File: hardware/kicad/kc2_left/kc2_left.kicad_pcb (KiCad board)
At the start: 2 copper layers, 145.7 x 132.2 mm, 76 parts, among them SW1 KEY_01, SW10 KEY_10, SW11 KEY_11, SW12 KEY_12, SW13 KEY_13, SW14 KEY_14, SW15 KEY_15, SW16 KEY_16, SW17 KEY_17, SW18 KEY_18, SW19 KEY_19, SW2 KEY_02, SW20 KEY_20, SW21 KEY_21, SW22 KEY_22, SW23 KEY_23, SW24 KEY_24, SW25 KEY_25, SW26 KEY_26, SW27 KEY_27, SW28 KEY_28, SW29 KEY_29, SW3 KEY_03, SW30 KEY_30, SW31 KEY_31, SW32 KEY_32, SW4 KEY_04, SW5 KEY_05, SW6 KEY_06, SW7 KEY_07, SW8 KEY_08, SW9 KEY_09, U1 nice!nano_v2_socket_24pin

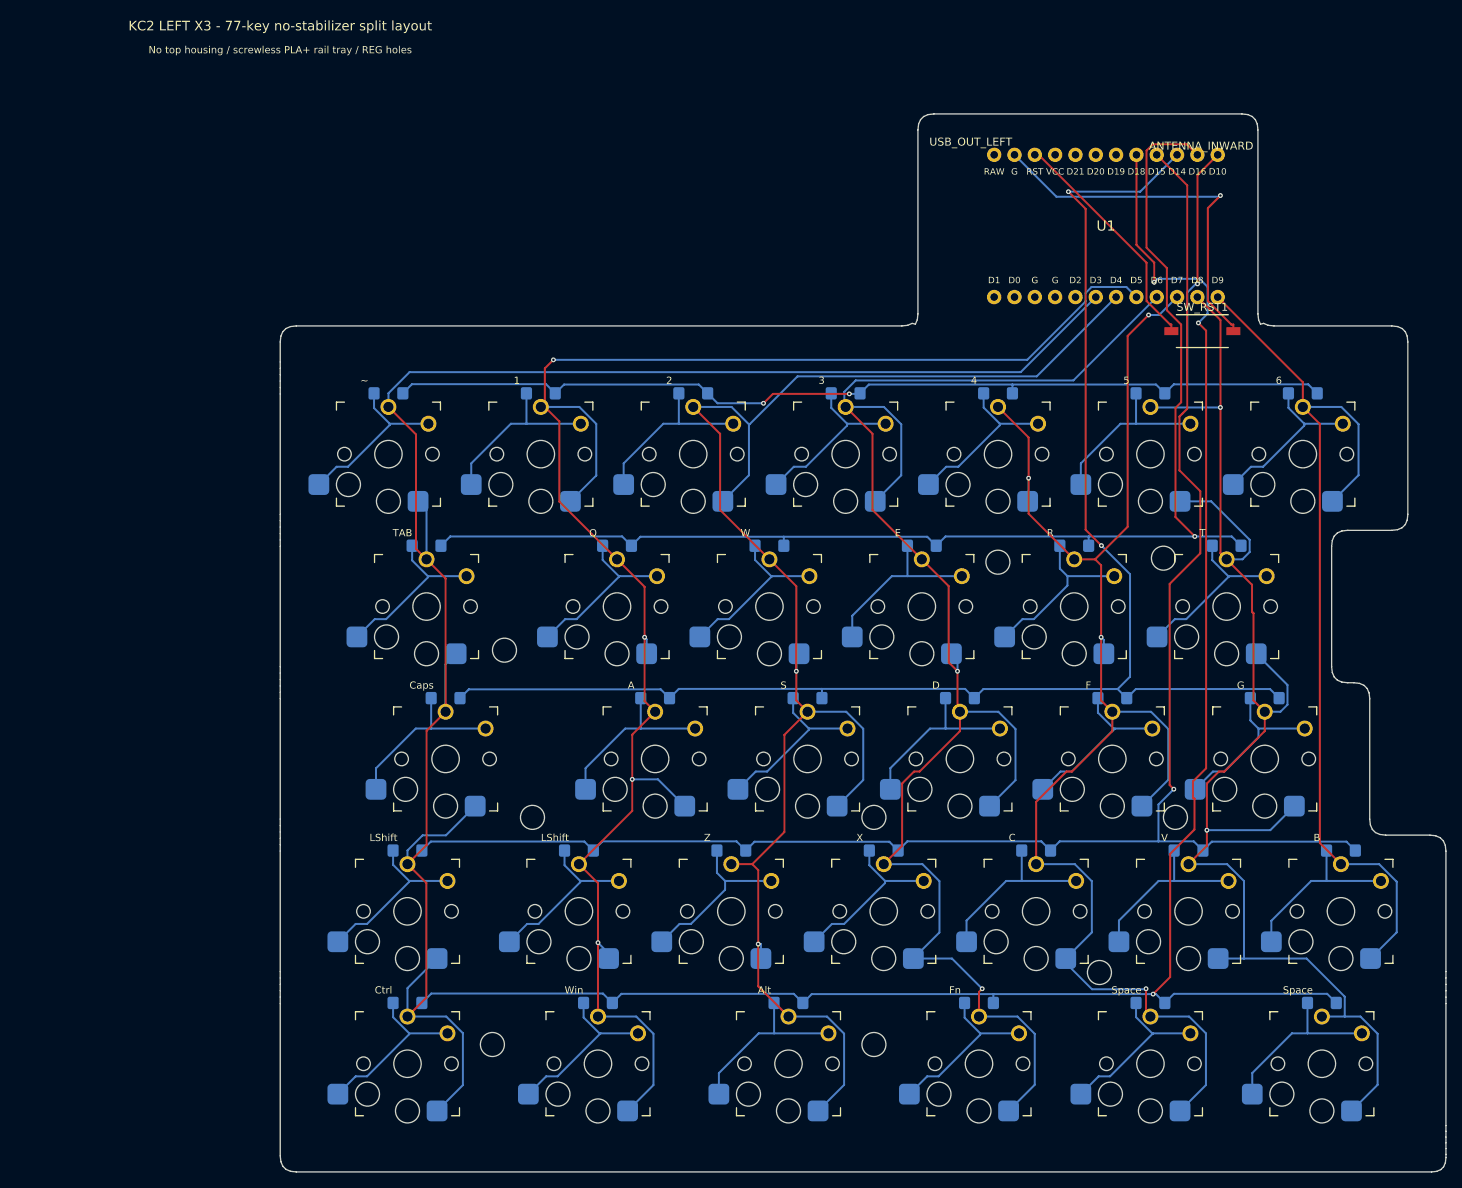
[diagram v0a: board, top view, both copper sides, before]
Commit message: feat(x3-v2): promote active hardware to canonical paths
Align PCB, housing, fabrication artifacts, firmware metadata, tooling, and SRS evidence with OPS-ARCH-006.

Keep fabrication blocked until physical evidence is complete.
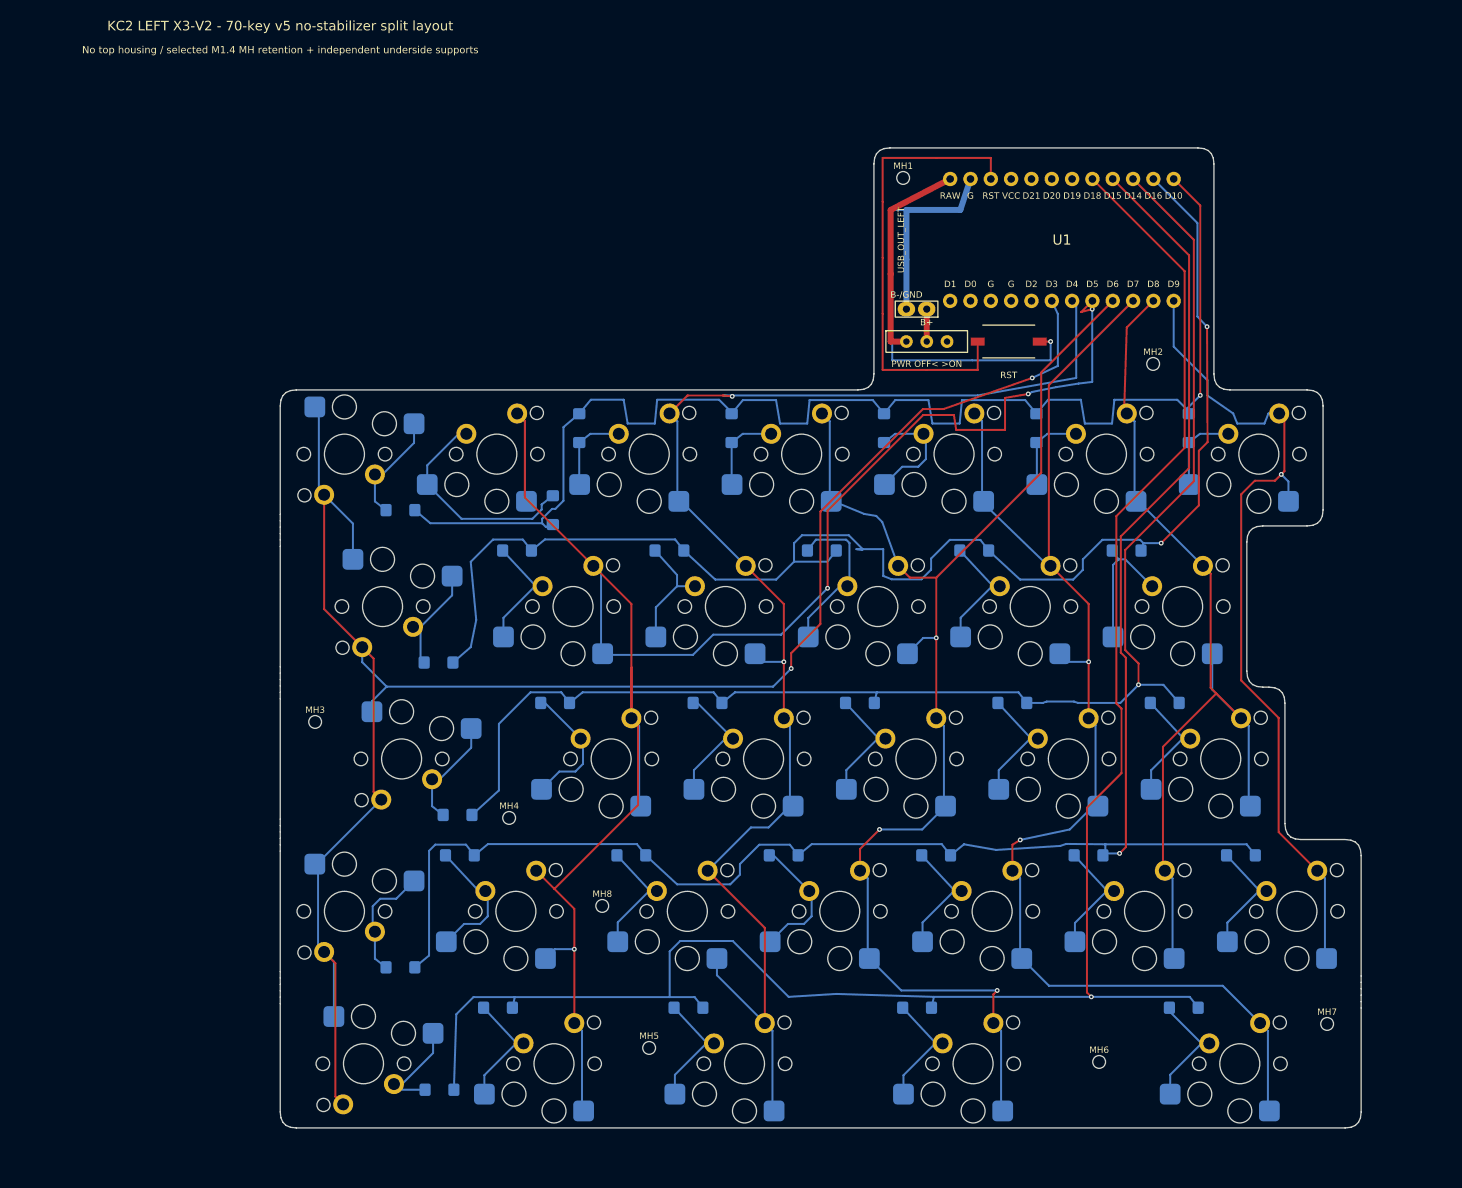
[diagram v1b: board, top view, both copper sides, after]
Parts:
- removed D32: 1N4148W_SOD123_DeviceMart_14592018, D_SOD123_HandSolder_14592018
- removed REG1, REG2, REG3, REG4, REG5, REG6, REG7, REG8, REG9: REG_NPTH_3.0, REG_NPTH_3.0
- removed SW32: KEY_32, SW_Kailh_Choc_V1_HotSwap_THT
- added BAT1: 301230_3.7V_100mAh, BAT_301230_30x12mm, F.Cu at (131.7, 50.8)
- added J_BAT1: 301230_DIRECT_SOLDER, BAT_2Pin_PTH_DirectSolder, F.Cu at (115.8, 59.4)
- added MH1: M1.4_NPTH_1.60, MH_M1.4_NPTH_1.60, F.Cu at (112.9, 43.0)
- added MH2: M1.4_NPTH_1.60, MH_M1.4_NPTH_1.60, F.Cu at (144.1, 66.2)
- added MH3: M1.4_NPTH_1.60, MH_M1.4_NPTH_1.60, F.Cu at (39.4, 111.0)
- added MH4: M1.4_NPTH_1.60, MH_M1.4_NPTH_1.60, F.Cu at (63.6, 123.0)
- added MH5: M1.4_NPTH_1.60, MH_M1.4_NPTH_1.60, F.Cu at (81.1, 151.8)
- added MH6: M1.4_NPTH_1.60, MH_M1.4_NPTH_1.60, F.Cu at (137.4, 153.5)
- added MH7: M1.4_NPTH_1.60, MH_M1.4_NPTH_1.60, F.Cu at (165.9, 148.8)
- added MH8: M1.4_NPTH_1.60, MH_M1.4_NPTH_1.60, F.Cu at (75.2, 134.0)
- added SW_PWR1: IMMS-12V_BSI-10, SW_IMMS_12V_BSI10_THT, F.Cu at (115.8, 63.5)
- D1, D10, D11, D12, D13, D14, D15, D16, D17, D18, D19, D2, D20, D21, D22, D23, D24, D25, D26, D27, D28, D29, D3, D30, D31, D4, D5, D6, D7, D8, D9: value 1N4148W_SOD123_DeviceMart_14592018 -> 1N4148W-13-F_DiodesInc_SOD123; footprint D_SOD123_HandSolder_14592018 -> D_1N4148W_SOD123_HandSolder_DiodesInc
- SW1, SW10, SW11, SW12, SW13, SW14, SW15, SW16, SW17, SW18, SW19, SW2, SW20, SW21, SW22, SW23, SW24, SW25, SW26, SW27, SW28, SW29, SW3, SW30, SW31, SW4, SW5, SW6, SW7, SW8, SW9: footprint SW_Kailh_Choc_V1_HotSwap_THT -> SW_Choc_V2_Socket_MX_THT
- moved BAT_LEAD_SLOT1 36.2 mm to (117.9, 50.8)
- moved SW_RST1 24.2 mm to (126.1, 63.5)
- moved D3 14.9 mm to (72.4, 74.3), turned to -90 degrees
- moved D4 14.9 mm to (91.4, 74.3), turned to -90 degrees
- moved D5 14.9 mm to (110.5, 74.3), turned to -90 degrees
- moved D6 14.9 mm to (129.5, 74.3), turned to -90 degrees
- moved D7 14.9 mm to (148.6, 74.3), turned to -90 degrees
- moved D21 14.9 mm to (57.5, 127.7)
- moved D1 14.7 mm to (50.0, 84.5)
- moved D2 14.7 mm to (69.1, 84.5), turned to 90 degrees
- moved D8 14.7 mm to (54.8, 103.6)
- moved D14 14.7 mm to (57.2, 122.6)
- moved D20 14.6 mm to (50.0, 141.7)
- moved D24 12.5 mm to (117.0, 127.7)
- moved D10 12.5 mm to (83.7, 89.6)
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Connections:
- U1 pad RAW: (no net) -> NN_B+
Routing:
- net L_COL5: track 183.2 -> 117.2 mm, vias 2 -> 0
- net L_COL3: track 205.0 -> 167.3 mm, vias 2 -> 3
- net RST: track 29.5 -> 58.1 mm
- net NN_B+: track 0.00 -> 26.8 mm
- net L_COL1: track 221.8 -> 245.0 mm
- net LK32_D: track 22.2 -> 0.00 mm
- net L_COL2: track 203.0 -> 181.6 mm
- net GND: track 47.0 -> 67.3 mm
- net L_ROW0: track 150.5 -> 168.3 mm, vias 3 -> 1
- net L_ROW1: track 163.7 -> 179.4 mm, vias 1 -> 2
- net L_COL4: track 184.2 -> 168.6 mm, vias 4 -> 2
- net L_ROW2: track 188.8 -> 176.4 mm, vias 2 -> 1
- net LK06_D: track 22.2 -> 10.6 mm
- net LK03_D: track 22.2 -> 10.6 mm
- net LK04_D: track 21.6 -> 10.6 mm
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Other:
- board size 145.7 x 132.2 mm -> 135.1 x 122.5 mm
- board text added: "BAT STRAIN RELIEF"
- board text added: "Diode: Diodes Inc 1N4148W-13-F SOD-123; pad 1 = row cathode"
- board text added: "KC2 LEFT X3-V2 - 70-key v5 no-stabilizer split layout"
- board text added: "KC2 X3 V2 L"
- board text added: "No top housing / selected M1.4 MH retention + independent underside supports"
- board text added: "PWR OFF< >ON"
- board text added: "RST"
- board text added: "X3 V2: Choc V2 socket OR rotated MX 5-pin direct solder; Choc V1 unsupported"
- board text removed: "BAT LEAD EXIT"
- board text removed: "Battery solders directly to nice!nano B+/B-; no carrier power pads"
- board text removed: "Diode fallback: 1N4148W SOD-123 because DO-35 conflicts with compact hybrid footprint"
- board text removed: "H1"
- board text removed: "H2"
- board text removed: "H3"
- board text removed: "H4"
- board text removed: "H5"
- board text removed: "H6"
- board text removed: "H7"
- board text removed: "H8"
- board text removed: "H9"
- board text removed: "KC2 LEFT X3 - 77-key no-stabilizer split layout"
- board text removed: "KC2 v1.0 L"
- board text removed: "No top housing / screwless PLA+ rail tray / REG holes"
- board text removed: "TW301525 80mAh"
- board text removed: "Win"
- board text removed: "X3: X2 electrical stack, no-stabilizer 77-key split layout"

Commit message: feat(kc2): add solid-floor housing and publish reviewed order guide
CON-ARCH-004/006, OPS-ARCH-007: retain enlarged solder lands and reviewed PCB release; add continuous floors, silicone-foot layouts, CAD/native regression evidence, exact order.md paths, and raw-byte-safe release publication.
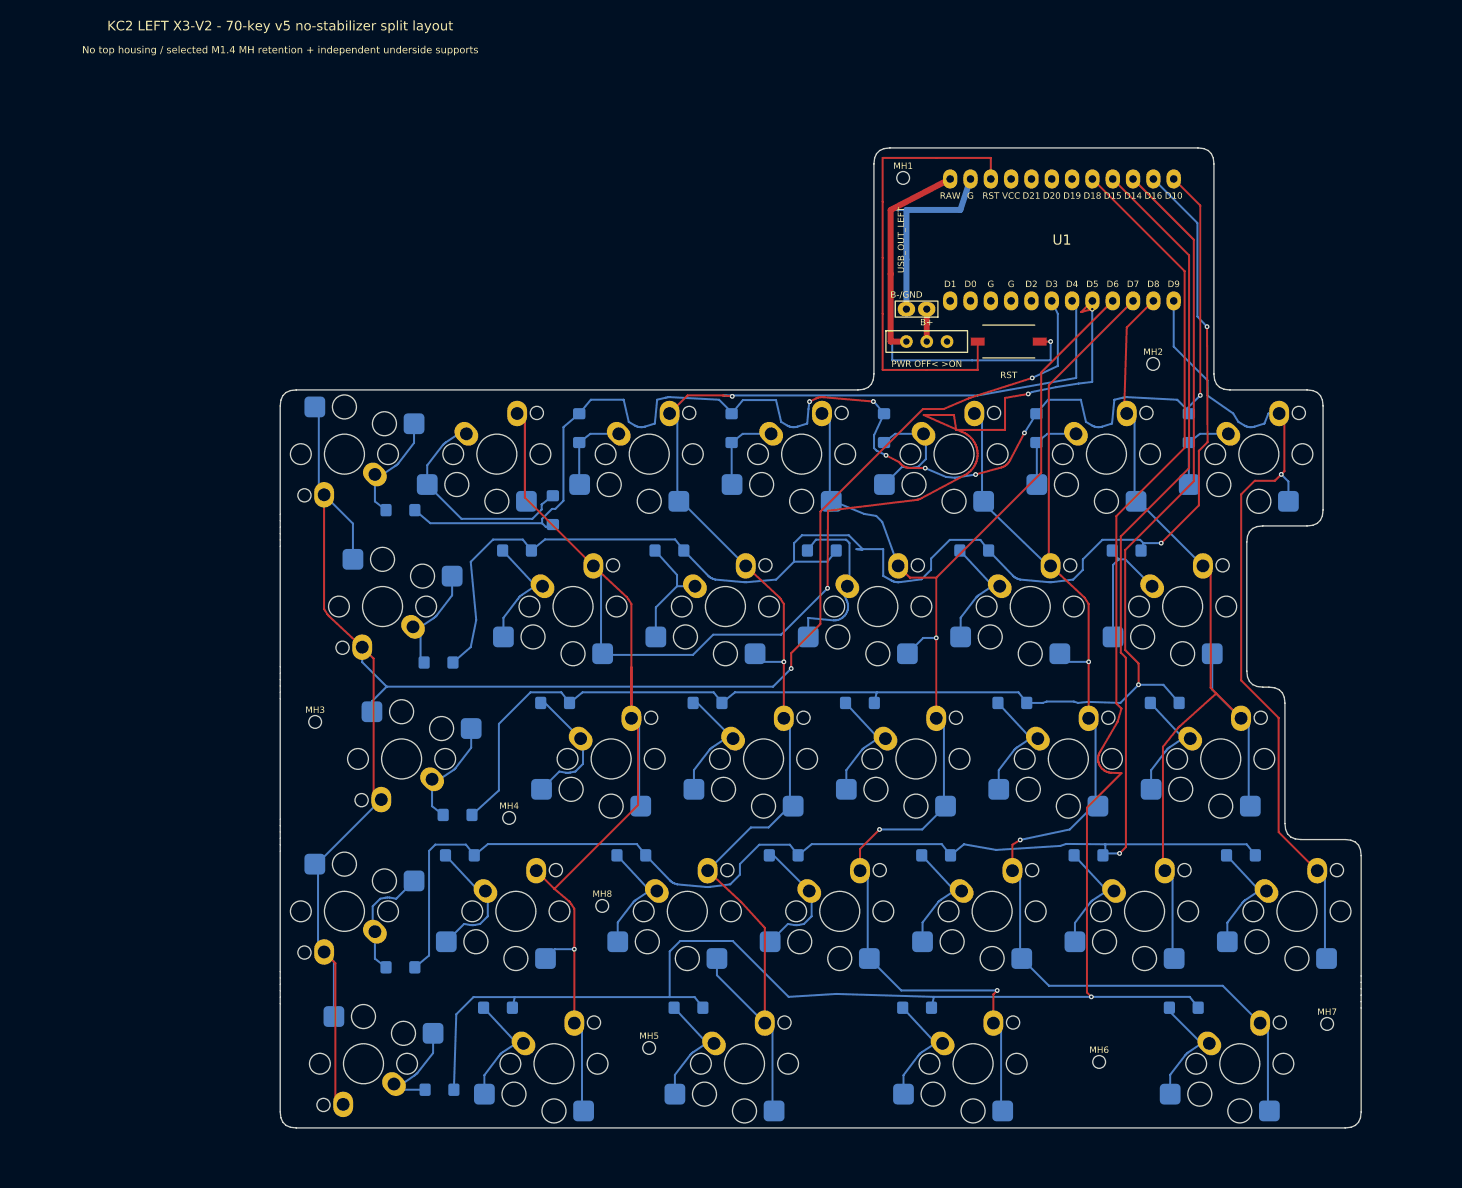
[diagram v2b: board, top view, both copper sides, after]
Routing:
- net L_COL1: track 245.0 -> 258.1 mm
- net L_ROW0: track 168.3 -> 172.7 mm, vias 1 -> 7
- net LK11_D: track 20.5 -> 23.6 mm
- net L_ROW4: track 233.3 -> 236.1 mm
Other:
- board text added: "X3 V2: Choc V1+ring / V2 socket OR MX direct solder / receptacles+plate; contact qualification pending"
- board text removed: "X3 V2: Choc V2 socket OR rotated MX 5-pin direct solder; Choc V1 unsupported"
